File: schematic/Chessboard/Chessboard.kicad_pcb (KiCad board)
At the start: 2 copper layers, 6 parts, among them Q1 BC640, U1 5V-3.3V

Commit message: edit schematics
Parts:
- removed A1: Arduino_Nano_ESP32, Module:Arduino_Nano
- added A2: Arduino_Nano_ESP32, Module:Arduino_Nano, F.Cu at (101.8, 79.4)
- added C1: 104, Capacitor_SMD:C_0603_1608Metric_Pad1.08x0.95mm_HandSolder, F.Cu at (146.1, 20.5)
- added C2: 104, Capacitor_SMD:C_0603_1608Metric_Pad1.08x0.95mm_HandSolder, F.Cu at (146.1, 23.0)
- added C3: C_Polarized, Capacitor_THT:CP_Radial_D14.0mm_P5.00mm, F.Cu at (189.5, 48.5)
- added D1: WS2812B, LED_SMD:LED_WS2812B_PLCC4_5.0x5.0mm_P3.2mm, F.Cu at (126.0, 22.0)
- added D2: WS2812B, LED_SMD:LED_WS2812B_PLCC4_5.0x5.0mm_P3.2mm, F.Cu at (136.0, 22.0)
- added H10: A3144, Package_TO_SOT_THT:TO-92_Inline, F.Cu at (24.9, 67.8)
- added H11: A3144, Package_TO_SOT_THT:TO-92_Inline, F.Cu at (24.9, 73.6)
- added H12: A3144, Package_TO_SOT_THT:TO-92_Inline, F.Cu at (31.4, 21.5)
- added H13: A3144, Package_TO_SOT_THT:TO-92_Inline, F.Cu at (31.4, 27.3)
- added H14: A3144, Package_TO_SOT_THT:TO-92_Inline, F.Cu at (31.4, 33.0)
- added H15: A3144, Package_TO_SOT_THT:TO-92_Inline, F.Cu at (31.4, 38.8)
- added H16: A3144, Package_TO_SOT_THT:TO-92_Inline, F.Cu at (31.4, 44.6)
- added H17: A3144, Package_TO_SOT_THT:TO-92_Inline, F.Cu at (31.4, 50.4)
- added H18: A3144, Package_TO_SOT_THT:TO-92_Inline, F.Cu at (31.4, 56.2)
- added H19: A3144, Package_TO_SOT_THT:TO-92_Inline, F.Cu at (31.4, 62.0)
- added H2: A3144, Package_TO_SOT_THT:TO-92_Inline, F.Cu at (24.9, 21.5)
- added H20: A3144, Package_TO_SOT_THT:TO-92_Inline, F.Cu at (31.4, 67.8)
- added H21: A3144, Package_TO_SOT_THT:TO-92_Inline, F.Cu at (31.4, 73.6)
- added H22: A3144, Package_TO_SOT_THT:TO-92_Inline, F.Cu at (38.0, 21.5)
- added H23: A3144, Package_TO_SOT_THT:TO-92_Inline, F.Cu at (38.0, 27.3)
- added H24: A3144, Package_TO_SOT_THT:TO-92_Inline, F.Cu at (38.0, 33.0)
- added H25: A3144, Package_TO_SOT_THT:TO-92_Inline, F.Cu at (38.0, 38.8)
- added H26: A3144, Package_TO_SOT_THT:TO-92_Inline, F.Cu at (38.0, 44.6)
- added H27: A3144, Package_TO_SOT_THT:TO-92_Inline, F.Cu at (38.0, 50.4)
- added H28: A3144, Package_TO_SOT_THT:TO-92_Inline, F.Cu at (38.0, 56.2)
- added H29: A3144, Package_TO_SOT_THT:TO-92_Inline, F.Cu at (38.0, 62.0)
- added H3: A3144, Package_TO_SOT_THT:TO-92_Inline, F.Cu at (24.9, 27.3)
- added H30: A3144, Package_TO_SOT_THT:TO-92_Inline, F.Cu at (38.0, 67.8)
- added H31: A3144, Package_TO_SOT_THT:TO-92_Inline, F.Cu at (38.0, 73.6)
- added H32: A3144, Package_TO_SOT_THT:TO-92_Inline, F.Cu at (44.5, 21.5)
- added H33: A3144, Package_TO_SOT_THT:TO-92_Inline, F.Cu at (44.5, 27.3)
- added H34: A3144, Package_TO_SOT_THT:TO-92_Inline, F.Cu at (44.5, 33.0)
- added H35: A3144, Package_TO_SOT_THT:TO-92_Inline, F.Cu at (44.5, 38.8)
- added H36: A3144, Package_TO_SOT_THT:TO-92_Inline, F.Cu at (44.5, 44.6)
- added H37: A3144, Package_TO_SOT_THT:TO-92_Inline, F.Cu at (44.5, 50.4)
- added H38: A3144, Package_TO_SOT_THT:TO-92_Inline, F.Cu at (44.5, 56.2)
- added H39: A3144, Package_TO_SOT_THT:TO-92_Inline, F.Cu at (44.5, 62.0)
- added H4: A3144, Package_TO_SOT_THT:TO-92_Inline, F.Cu at (24.9, 33.0)
- added H40: A3144, Package_TO_SOT_THT:TO-92_Inline, F.Cu at (44.5, 67.8)
- added H41: A3144, Package_TO_SOT_THT:TO-92_Inline, F.Cu at (44.5, 73.6)
- added H42: A3144, Package_TO_SOT_THT:TO-92_Inline, F.Cu at (51.0, 21.5)
- added H43: A3144, Package_TO_SOT_THT:TO-92_Inline, F.Cu at (51.0, 27.3)
- added H44: A3144, Package_TO_SOT_THT:TO-92_Inline, F.Cu at (51.0, 33.0)
- added H45: A3144, Package_TO_SOT_THT:TO-92_Inline, F.Cu at (51.0, 38.8)
- added H46: A3144, Package_TO_SOT_THT:TO-92_Inline, F.Cu at (51.0, 44.6)
- added H47: A3144, Package_TO_SOT_THT:TO-92_Inline, F.Cu at (51.0, 50.4)
- added H48: A3144, Package_TO_SOT_THT:TO-92_Inline, F.Cu at (51.0, 56.2)
- added H49: A3144, Package_TO_SOT_THT:TO-92_Inline, F.Cu at (51.0, 62.0)
- added H5: A3144, Package_TO_SOT_THT:TO-92_Inline, F.Cu at (24.9, 38.8)
- added H50: A3144, Package_TO_SOT_THT:TO-92_Inline, F.Cu at (51.0, 67.8)
- added H51: A3144, Package_TO_SOT_THT:TO-92_Inline, F.Cu at (51.0, 73.6)
- added H52: A3144, Package_TO_SOT_THT:TO-92_Inline, F.Cu at (57.5, 21.5)
- added H53: A3144, Package_TO_SOT_THT:TO-92_Inline, F.Cu at (57.5, 27.3)
- added H54: A3144, Package_TO_SOT_THT:TO-92_Inline, F.Cu at (57.5, 33.0)
- added H55: A3144, Package_TO_SOT_THT:TO-92_Inline, F.Cu at (57.5, 38.8)
- added H56: A3144, Package_TO_SOT_THT:TO-92_Inline, F.Cu at (57.5, 44.6)
- added H57: A3144, Package_TO_SOT_THT:TO-92_Inline, F.Cu at (57.5, 50.4)
- added H58: A3144, Package_TO_SOT_THT:TO-92_Inline, F.Cu at (57.5, 56.2)
- added H59: A3144, Package_TO_SOT_THT:TO-92_Inline, F.Cu at (57.5, 62.0)
- added H6: A3144, Package_TO_SOT_THT:TO-92_Inline, F.Cu at (24.9, 44.6)
- added H60: A3144, Package_TO_SOT_THT:TO-92_Inline, F.Cu at (57.5, 67.8)
- added H61: A3144, Package_TO_SOT_THT:TO-92_Inline, F.Cu at (57.5, 73.6)
- added H62: A3144, Package_TO_SOT_THT:TO-92_Inline, F.Cu at (64.0, 21.5)
- added H63: A3144, Package_TO_SOT_THT:TO-92_Inline, F.Cu at (64.0, 27.3)
- added H64: A3144, Package_TO_SOT_THT:TO-92_Inline, F.Cu at (64.0, 33.0)
- added H7: A3144, Package_TO_SOT_THT:TO-92_Inline, F.Cu at (24.9, 50.4)
- added H8: A3144, Package_TO_SOT_THT:TO-92_Inline, F.Cu at (24.9, 56.2)
- added H9: A3144, Package_TO_SOT_THT:TO-92_Inline, F.Cu at (24.9, 62.0)
- added J1: LED, Connector_JST:JST_XH_B3B-XH-A_1x03_P2.50mm_Vertical, F.Cu at (169.4, 109.3)
- added J2: VOUT, Connector_JST:JST_XH_B4B-XH-A_1x04_P2.50mm_Vertical, F.Cu at (155.0, 93.8)
- added J3: Data, Connector_JST:JST_XH_B5B-XH-A_1x05_P2.50mm_Vertical, F.Cu at (155.0, 86.0)
- added J4: VOUT, Connector_JST:JST_XH_B4B-XH-A_1x04_P2.50mm_Vertical, F.Cu at (155.0, 101.6)
- added J5: Data, Connector_JST:JST_XH_B4B-XH-A_1x04_P2.50mm_Vertical, F.Cu at (155.0, 109.4)
- added Q2: BC640, Package_TO_SOT_THT:TO-92_Inline, F.Cu at (92.8, 71.8)
- added Q3: BC640, Package_TO_SOT_THT:TO-92_Inline, F.Cu at (166.0, 28.4)
- added Q4: BC640, Package_TO_SOT_THT:TO-92_Inline, F.Cu at (166.0, 34.2)
- added Q5: BC640, Package_TO_SOT_THT:TO-92_Inline, F.Cu at (166.0, 40.0)
- added Q6: BC640, Package_TO_SOT_THT:TO-92_Inline, F.Cu at (166.0, 45.8)
- added Q7: BC640, Package_TO_SOT_THT:TO-92_Inline, F.Cu at (166.0, 51.6)
- added Q8: BC640, Package_TO_SOT_THT:TO-92_Inline, F.Cu at (166.0, 57.4)
- added R3: 2K2, Resistor_THT:R_Axial_DIN0207_L6.3mm_D2.5mm_P10.16mm_Horizontal, F.Cu at (172.1, 42.7)
- added R4: 2K2, Resistor_THT:R_Axial_DIN0207_L6.3mm_D2.5mm_P10.16mm_Horizontal, F.Cu at (172.1, 46.8)
- added R5: 2K2, Resistor_THT:R_Axial_DIN0207_L6.3mm_D2.5mm_P10.16mm_Horizontal, F.Cu at (172.1, 50.8)
- added R6: 2K2, Resistor_THT:R_Axial_DIN0207_L6.3mm_D2.5mm_P10.16mm_Horizontal, F.Cu at (172.1, 54.9)
- added R7: 2K2, Resistor_THT:R_Axial_DIN0207_L6.3mm_D2.5mm_P10.16mm_Horizontal, F.Cu at (172.1, 58.9)
- added R8: 2K2, Resistor_THT:R_Axial_DIN0207_L6.3mm_D2.5mm_P10.16mm_Horizontal, F.Cu at (172.1, 63.0)
- added SW1: SW_SPST, Connector_PinHeader_2.54mm:PinHeader_1x02_P2.54mm_Vertical, F.Cu at (177.0, 83.5)
- added U2: Batterie Shield, Library:D1_mini_board, F.Cu at (74.5, 103.0)
- added U3: Logic Level Shifter, Library:LogicLevel4ch, F.Cu at (135.0, 92.8)
- added U4: Logic Level Shifter, Library:LogicLevel4ch, F.Cu at (177.4, 34.2)
- added U5: Logic Level Shifter, Library:LogicLevel4ch, F.Cu at (191.2, 34.2)
- H1: value SS49E -> A3144
- R1: value 10K -> 2K2
- U1: value 5V-3.3V -> Logic Level Shifter; footprint Converter_DCDC:Converter_DCDC_Murata_OKI-78SR_Vertical -> Library:LogicLevel4ch
- moved U1 98.2 mm to (135.0, 114.5)
- moved R2 67.6 mm to (126.9, 74.0)
- moved Q1 65.4 mm to (118.7, 68.9)
- moved H1 53.6 mm to (110.0, 22.4)
- moved R1 46.4 mm to (92.3, 66.5)
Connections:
- net Net-(H1-VCC) renamed /Sensor/VS1
- H1 pad 3: Net-(A1-A0) -> /Sensor/D1
- Q1 pad 1: +3V3 -> +5V
- R1 pad 1: Net-(A1-A0) -> Net-(Q2-B)
- R1 pad 2: GND -> Net-(U3-HV2)
- U1 pad 1: +5V -> /Sensor/D1
- U1 pad 2: +3V3 -> /Sensor/D2
- U1 pad 3: GND -> +5V

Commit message: routen and gerber files
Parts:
- removed C1, C2: 104, Capacitor_SMD:C_0603_1608Metric_Pad1.08x0.95mm_HandSolder
- removed D1, D2: WS2812B, LED_SMD:LED_WS2812B_PLCC4_5.0x5.0mm_P3.2mm
- removed H1, H10, H11, H12, H13, H14, H15, H16, H17, H18, H19, H2, H20, H21, H22, H23, H24, H25, H26, H27, H28, H29, H3, H30, H31, H32, H33, H34, H35, H36, H37, H38, H39, H4, H40, H41, H42, H43, H44, H45, H46, H47, H48, H49, H5, H50, H51, H52, H53, H54, H55, H56, H57, H58, H59, H6, H60, H61, H62, H63, H64, H7, H8, H9: A3144, Package_TO_SOT_THT:TO-92_Inline
- moved U5 102.5 mm to (118.9, 106.9)
- moved U2 91.0 mm to (165.5, 103.2)
- moved C3 77.6 mm to (116.5, 74.7)
- moved J1 59.1 mm to (170.0, 50.2), turned to -90 degrees
- moved Q2 50.8 mm to (142.5, 61.2), turned to -90 degrees
- moved SW1 48.7 mm to (155.5, 39.7), turned to 90 degrees
- moved J4 48.0 mm to (152.0, 53.7), turned to 90 degrees
- moved R8 46.4 mm to (131.0, 41.5), turned to 180 degrees
- moved R3 44.2 mm to (131.0, 59.0), turned to 180 degrees
- moved R7 43.4 mm to (131.0, 45.0), turned to 180 degrees
- moved J5 43.2 mm to (171.6, 69.6), turned to 90 degrees
- moved R4 42.0 mm to (131.0, 55.5), turned to 180 degrees
- moved R6 41.6 mm to (131.0, 48.5), turned to 180 degrees
- moved U1 41.3 mm to (161.1, 82.4), turned to 180 degrees
- moved Q3 41.2 mm to (137.0, 57.7), turned to -90 degrees
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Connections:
- net /LED/LED_Data renamed /LED_ROW_1_2/LED_Data
- Q5 pad 2: /Sensor/VS6 -> /Sensor/VS5
- Q6 pad 2: /Sensor/VS5 -> /Sensor/VS6
- Q7 pad 2: /Sensor/VS8 -> /Sensor/VS7
- Q8 pad 2: /Sensor/VS7 -> /Sensor/VS8
- R1 pad 1: Net-(Q2-B) -> Net-(Q1-B)
- R1 pad 2: Net-(U3-HV2) -> Net-(U3-HV1)
- R2 pad 1: Net-(Q1-B) -> Net-(Q2-B)
- R2 pad 2: Net-(U3-HV1) -> Net-(U3-HV2)
- R5 pad 2: Net-(U5-HV2) -> Net-(U5-HV1)
- R6 pad 2: Net-(U5-HV1) -> Net-(U5-HV2)
- R7 pad 2: Net-(U5-HV4) -> Net-(U5-HV3)
- R8 pad 2: Net-(U5-HV3) -> Net-(U5-HV4)
- U1 pad 11: Net-(A2-A6) -> Net-(A2-A1)
- U1 pad 12: Net-(A2-A7) -> Net-(A2-A0)
- U1 pad 7: Net-(A2-SDA/A4) -> Net-(A2-A3)
- U1 pad 8: Net-(A2-SCL/A5) -> Net-(A2-A2)
- U4 pad 11: Net-(A2-A2) -> Net-(A2-SCL/A5)
- U4 pad 12: Net-(A2-A3) -> Net-(A2-SDA/A4)
- U4 pad 7: Net-(A2-A0) -> Net-(A2-A7)
- U4 pad 8: Net-(A2-A1) -> Net-(A2-A6)
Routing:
- net +5V: track 0.00 -> 350.1 mm
- net GND: track 0.00 -> 170.1 mm
- net +3V3: track 0.00 -> 112.6 mm
- net Net-(SW1-B): track 0.00 -> 81.7 mm
- net Net-(U5-HV4): track 0.00 -> 78.2 mm
- net Net-(U5-HV3): track 0.00 -> 71.8 mm
- net /LED_ROW_1_2/LED_Data: track 0.00 -> 63.4 mm
- net Net-(U5-HV2): track 0.00 -> 59.9 mm
- net Net-(U5-HV1): track 0.00 -> 53.3 mm
- net Net-(U3-HV4): track 0.00 -> 46.2 mm
- net Net-(U3-HV3): track 0.00 -> 39.8 mm
- net /Sensor/VS1: track 0.00 -> 30.1 mm
- net Net-(A2-A6): track 0.00 -> 29.7 mm
- net Net-(A2-A7): track 0.00 -> 28.8 mm
- net /Sensor/VS3: track 0.00 -> 28.8 mm
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
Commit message: finish Mainboard design
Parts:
- added ?: , , F.Cu at (113.0, 118.5)
- added ?: , , F.Cu at (177.0, 42.5)
- added ?: , , F.Cu at (113.0, 42.5)
- added REF**: MountingHole_3.2mm_M3, MountingHole:MountingHole_3.2mm_M3, F.Cu at (177.0, 118.5)
- moved SW1 16.2 mm to (171.0, 44.5)
- moved Q1 4.84 mm to (141.6, 66.2)
- moved R1 4.84 mm to (135.6, 67.5)
- moved R2 4.84 mm to (135.6, 64.0)
- moved R3 4.84 mm to (135.6, 60.5)
- moved R4 4.84 mm to (135.6, 57.0)
- moved R5 4.84 mm to (135.6, 53.5)
- moved R6 4.84 mm to (135.6, 50.0)
- moved R7 4.84 mm to (135.6, 46.5)
- moved R8 4.84 mm to (135.6, 43.0)
- moved Q2 4.84 mm to (147.1, 62.7)
- moved Q3 4.84 mm to (141.6, 59.2)
- moved Q4 4.84 mm to (147.1, 55.7)
- moved Q5 4.84 mm to (141.6, 52.2)
- moved Q6 4.84 mm to (147.1, 49.2)
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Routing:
- net GND: track 170.1 -> 55.6 mm
- net Net-(A2-A7): track 28.8 -> 115.0 mm
- net Net-(A2-A6): track 29.7 -> 106.7 mm
- net Net-(A2-SCL/A5): track 26.3 -> 92.2 mm
- net Net-(A2-SDA/A4): track 26.7 -> 84.0 mm
- net +5V: track 350.1 -> 295.7 mm
- net Net-(A2-A3): track 24.7 -> 74.8 mm
- net Net-(A2-A2): track 25.2 -> 66.4 mm
- net Net-(A2-A1): track 20.1 -> 52.1 mm
- net Net-(A2-A0): track 20.2 -> 42.6 mm
- net +3V3: track 112.6 -> 90.9 mm
- net Net-(U5-HV3): track 71.8 -> 89.5 mm
- net Net-(U5-HV4): track 78.2 -> 94.2 mm
- net Net-(SW1-B): track 81.7 -> 66.7 mm
- net /LED_ROW_1_2/LED_Data: track 63.4 -> 56.7 mm
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- added copper zone on B.Cu, net GND
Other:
- board outline added: 70 x 81 mm
- board text added: "Chessboard"
- board text added: "Mainboard v1.0"
- board text added: "Mathias H."

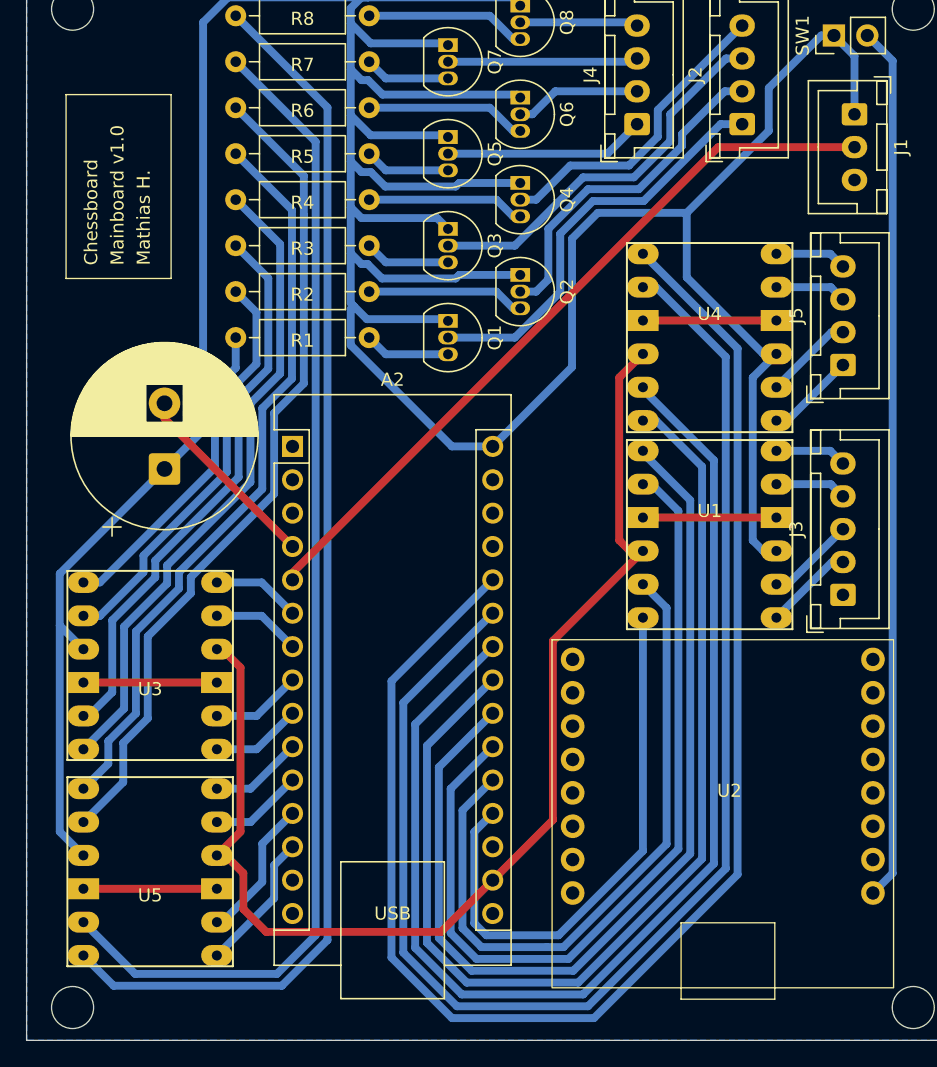
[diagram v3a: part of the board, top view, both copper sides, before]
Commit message: add left and right input field
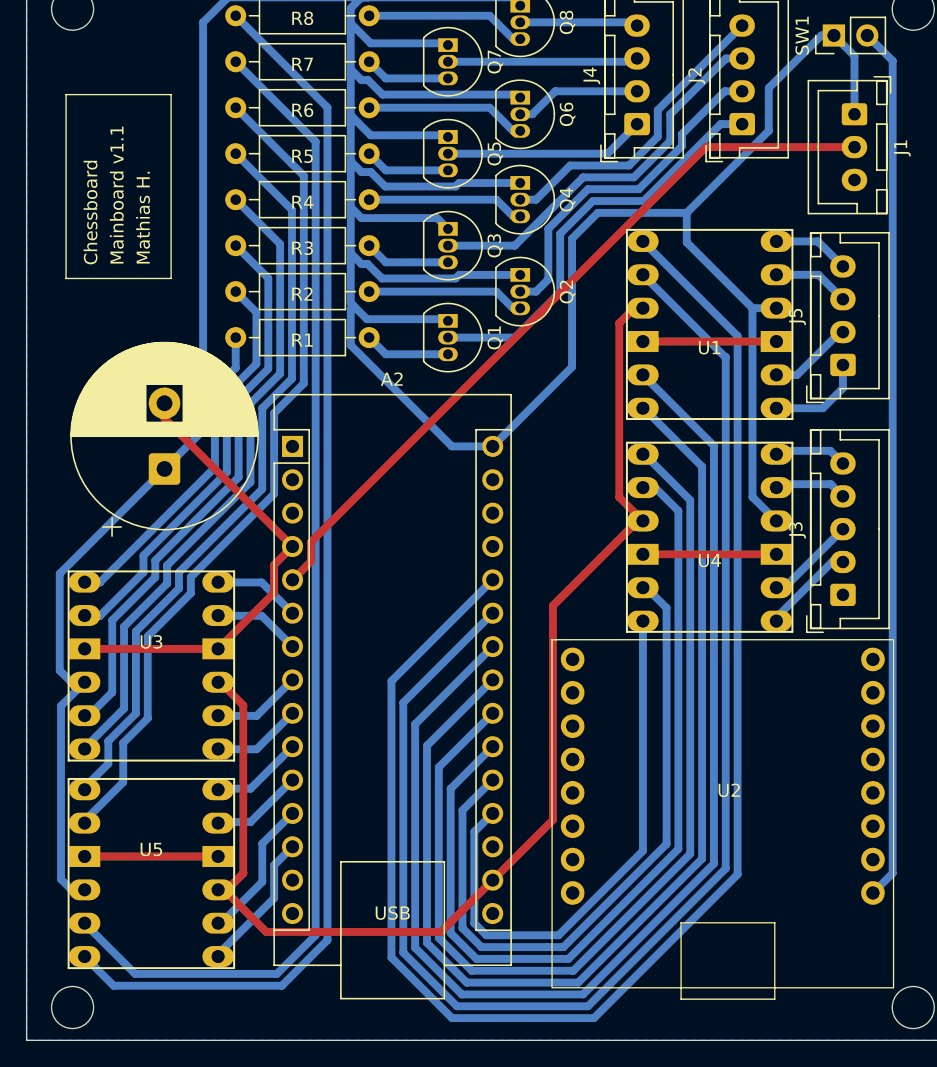
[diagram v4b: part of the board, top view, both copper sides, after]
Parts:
- moved U4 17.8 mm to (161.5, 84.0), turned to 0 degrees
- moved U1 13.4 mm to (161.5, 67.8), turned to 0 degrees
- moved U3 2.56 mm to (119.0, 91.2), turned to 180 degrees
- moved U5 2.46 mm to (119.0, 107.0), turned to 180 degrees
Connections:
- J3 pad 2: /Sensor/D1 -> /Sensor/D5
- J3 pad 3: /Sensor/D2 -> /Sensor/D6
- J3 pad 4: /Sensor/D3 -> /Sensor/D7
- J3 pad 5: /Sensor/D4 -> /Sensor/D8
- J5 pad 1: /Sensor/D5 -> /Sensor/D1
- J5 pad 2: /Sensor/D6 -> /Sensor/D2
- J5 pad 3: /Sensor/D7 -> /Sensor/D3
- J5 pad 4: /Sensor/D8 -> /Sensor/D4
- R1 pad 2: Net-(U3-HV1) -> Net-(U3-HV4)
- R2 pad 2: Net-(U3-HV2) -> Net-(U3-HV3)
- R3 pad 2: Net-(U3-HV3) -> Net-(U3-HV2)
- R4 pad 2: Net-(U3-HV4) -> Net-(U3-HV1)
- R5 pad 2: Net-(U5-HV1) -> Net-(U5-HV4)
- R6 pad 2: Net-(U5-HV2) -> Net-(U5-HV3)
- R7 pad 2: Net-(U5-HV3) -> Net-(U5-HV2)
- R8 pad 2: Net-(U5-HV4) -> Net-(U5-HV1)
- U1 pad 1: /Sensor/D1 -> /Sensor/D4
- U1 pad 11: Net-(A2-A1) -> Net-(A2-A6)
- U1 pad 12: Net-(A2-A0) -> Net-(A2-A7)
- U1 pad 2: /Sensor/D2 -> /Sensor/D3
- U1 pad 5: /Sensor/D3 -> /Sensor/D2
- U1 pad 6: /Sensor/D4 -> /Sensor/D1
- U1 pad 7: Net-(A2-A3) -> Net-(A2-SDA/A4)
- U1 pad 8: Net-(A2-A2) -> Net-(A2-SCL/A5)
- U3 pad 11: Net-(A2-D4) -> Net-(A2-D5)
- U3 pad 12: Net-(A2-D3) -> Net-(A2-D6)
- U3 pad 7: Net-(A2-D6) -> Net-(A2-D3)
- U3 pad 8: Net-(A2-D5) -> Net-(A2-D4)
- U4 pad 1: /Sensor/D5 -> /Sensor/D8
- U4 pad 11: Net-(A2-SCL/A5) -> Net-(A2-A2)
- U4 pad 12: Net-(A2-SDA/A4) -> Net-(A2-A3)
- U4 pad 2: /Sensor/D6 -> /Sensor/D7
- U4 pad 5: /Sensor/D7 -> /Sensor/D6
- U4 pad 6: /Sensor/D8 -> /Sensor/D5
- U4 pad 7: Net-(A2-A7) -> Net-(A2-A0)
- U4 pad 8: Net-(A2-A6) -> Net-(A2-A1)
- U5 pad 11: Net-(A2-D8) -> Net-(A2-D9)
- U5 pad 12: Net-(A2-D7) -> Net-(A2-D10/CS)
- U5 pad 7: Net-(A2-D10/CS) -> Net-(A2-D7)
- U5 pad 8: Net-(A2-D9) -> Net-(A2-D8)
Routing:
- net Net-(U5-HV4): track 94.2 -> 56.7 mm
- net Net-(U5-HV1): track 56.7 -> 94.2 mm
- net Net-(U5-HV3): track 89.5 -> 63.8 mm
- net Net-(U5-HV2): track 63.8 -> 89.5 mm
- net Net-(U3-HV1): track 24.2 -> 49.4 mm
- net Net-(U3-HV4): track 49.4 -> 26.5 mm
- net GND: track 55.6 -> 67.8 mm
- net Net-(U3-HV2): track 31.5 -> 42.9 mm
- net Net-(U3-HV3): track 42.9 -> 33.9 mm
- net /LED_ROW_1_2/LED_Data: track 56.7 -> 57.8 mm
- net Net-(A2-SCL/A5): track 92.2 -> 93.2 mm
- net Net-(A2-A7): track 115.0 -> 115.9 mm
- net +3V3: track 90.9 -> 91.7 mm
- net /Sensor/D1: track 6.82 -> 7.47 mm
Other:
- board text added: "Mainboard v1.1"
- board text removed: "Mainboard v1.0"
